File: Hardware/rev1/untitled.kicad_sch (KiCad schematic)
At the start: 16 parts, among them J2 USB_C_Receptacle_USB2.0_14P, J3 Screw_Terminal_01x02, U2 HT75xx-1-SOT89

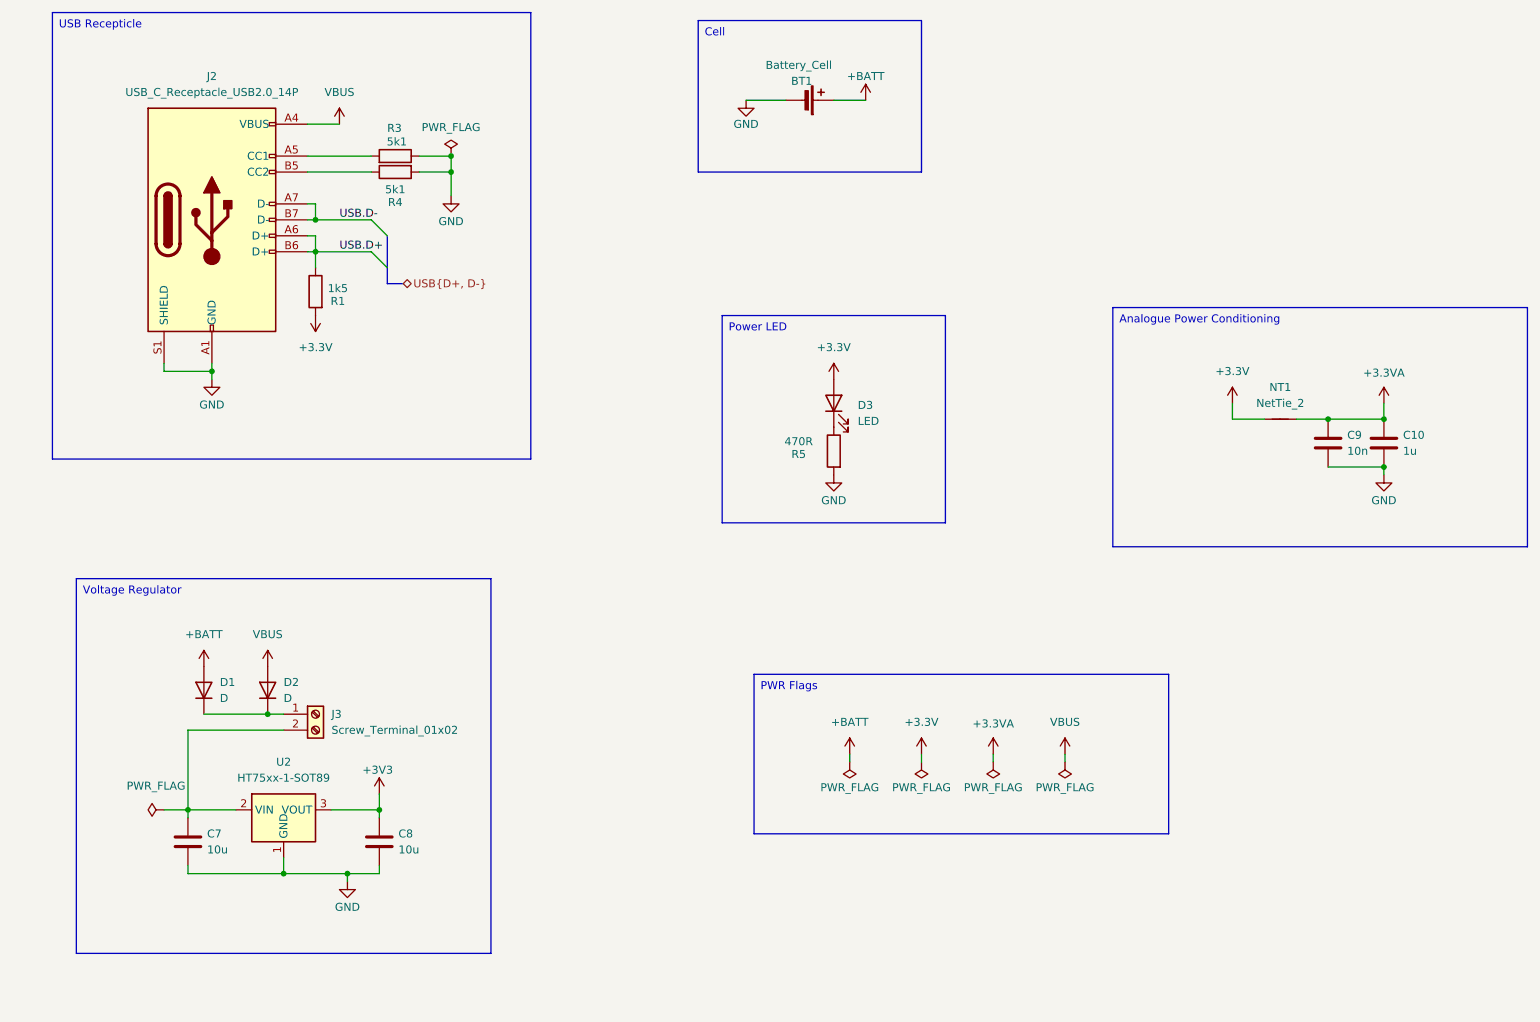
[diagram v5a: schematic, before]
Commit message: Literal Progress
PCB populated, schematic changed, all pins on MCU accessible from headers, all components on board, traces required
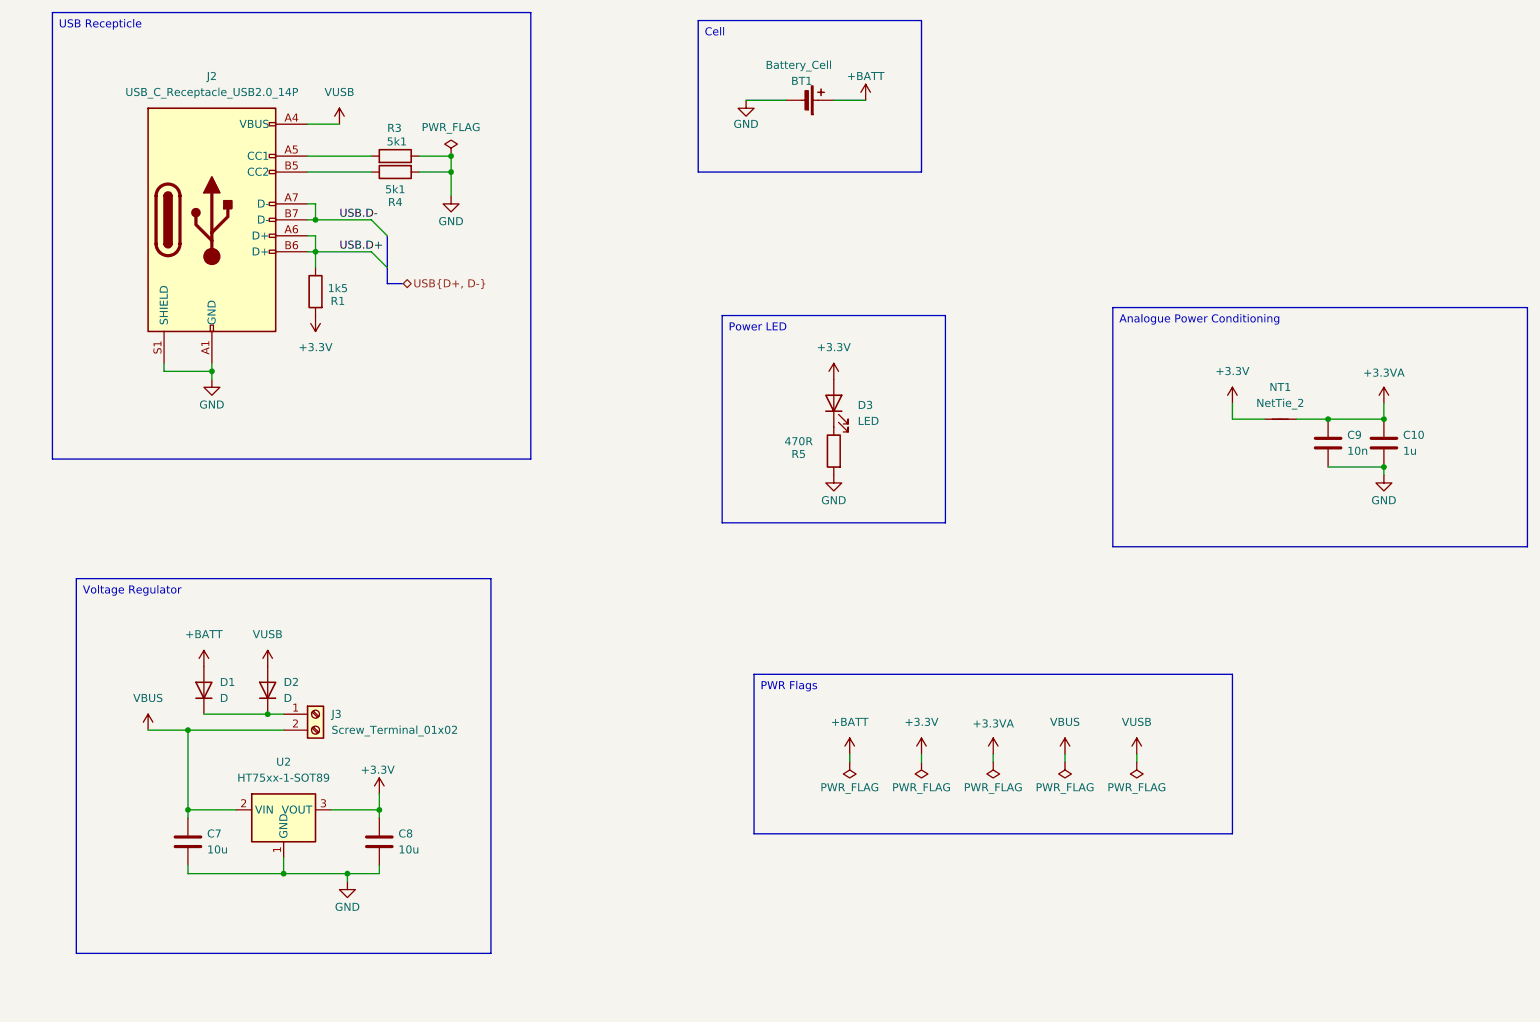
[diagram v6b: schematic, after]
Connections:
- net +3V3 is gone; now on net +3.3V: C8.1, U2.3 (VOUT)
- net VBUS: now also C7.1, J3.2 (Pin_2), U2.2 (VIN); no longer D2.2 (A), J2.A4 (VBUS), J2.A9 (VBUS), J2.B4 (VBUS), J2.B9 (VBUS)
- new net VUSB: D2.2 (A), J2.A4 (VBUS), J2.A9 (VBUS), J2.B4 (VBUS), J2.B9 (VBUS)
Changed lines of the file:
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@@
 	)
 	(junction
+		(at 54.61 140.97)
+		(diameter 0)
+		(color 0 0 0 0)
+	)
+	(junction
 		(at 85.09 153.67)
 		(diameter 0)
@@
 	(wire
 		(pts
+			(xy 205.74 144.78) (xy 205.74 146.05)
+		)
+		(stroke
+			(width 0)
+			(type default)
+		)
+	)
+	(wire
+		(pts
 			(xy 73.66 49.53) (xy 83.82 49.53)
 		)
@@
 	(wire
 		(pts
-			(xy 50.8 153.67) (xy 54.61 153.67)
-		)
-		(stroke
-			(width 0)
-			(type default)
-		)
-	)
-	(wire
-		(pts
 			(xy 50.8 83.82) (xy 58.42 83.82)
 		)
@@
 		)
 	)
+	(wire
+		(pts
+			(xy 48.26 140.97) (xy 54.61 140.97)
+		)
+		(stroke
+			(width 0)
+			(type default)
+		)
+	)
 	(text_box "Analogue Power Conditioning"
 		(exclude_from_sim no)
@@
 		(exclude_from_sim no)
 		(at 144.78 132.08 0)
-		(size 66.04 25.4)
+		(size 76.2 25.4)
 		(stroke
 			(width 0)
@@
 			)
 		)
-		(property "Value" "VBUS"
+		(property "Value" "VUSB"
 			(at 67.31 125.73 0)
 			(effects
@@
 			)
 		)
-		(property "Value" "+3V3"
+		(property "Value" "+3.3V"
 			(at 84.836 147.32 0)
 			(effects
@@
 	)
 	(symbol
-		(lib_id "power:PWR_FLAG")
-		(at 50.8 153.67 90)
-		(unit 1)
-		(exclude_from_sim no)
-		(in_bom yes)
-		(on_board yes)
-		(dnp no)
-		(fields_autoplaced yes)
-		(property "Reference" "#FLG01"
-			(at 48.895 153.67 0)
-			(effects
-				(font
-					(size 1.27 1.27)
-				)
-				(hide yes)
-			)
-		)
-		(property "Value" "PWR_FLAG"
-			(at 49.53 149.86 90)
-			(effects
-				(font
-					(size 1.27 1.27)
-				)
-			)
-		)
-		(property "Footprint" ""
-			(at 50.8 153.67 0)
-			(effects
-				(font
-					(size 1.27 1.27)
-				)
-				(hide yes)
-			)
-		)
-		(property "Datasheet" "~"
-			(at 50.8 153.67 0)
-			(effects
-				(font
-					(size 1.27 1.27)
-				)
-				(hide yes)
-			)
-		)
-		(property "Description" "Special symbol for telling ERC where power comes from"
-			(at 50.8 153.67 0)
-			(effects
-				(font
-					(size 1.27 1.27)
-				)
-				(hide yes)
-			)
-		)
-		(pin "1"
-		)
-		(instances
-			(project "rev1"
-				(path "/e52639ab-1647-4d34-8bc5-5aadc4708147/28e3f1a4-a9ec-420d-b6dc-1cdf5f0e43fa"
-					(reference "#FLG01")
-					(unit 1)
-				)
-			)
-		)
-	)
-	(symbol
 		(lib_id "power:+3.3V")
 		(at 157.48 85.09 0)
@@
 	)
 	(symbol
+		(lib_id "power:VBUS")
+		(at 48.26 140.97 0)
+		(unit 1)
+		(exclude_from_sim no)
+		(in_bom yes)
+		(on_board yes)
+		(dnp no)
+		(fields_autoplaced yes)
+		(property "Reference" "#PWR043"
+			(at 48.26 144.78 0)
+			(effects
+				(font
+					(size 1.27 1.27)
+				)
+				(hide yes)
+			)
+		)
+		(property "Value" "VBUS"
+			(at 48.26 135.89 0)
+			(effects
+				(font
+					(size 1.27 1.27)
+				)
+			)
+		)
+		(property "Footprint" ""
+			(at 48.26 140.97 0)
+			(effects
+				(font
+					(size 1.27 1.27)
+				)
+				(hide yes)
+			)
+		)
+		(property "Datasheet" ""
+			(at 48.26 140.97 0)
+			(effects
+				(font
+					(size 1.27 1.27)
+				)
+				(hide yes)
+			)
+		)
+		(property "Description" "Power symbol creates a global label with name \"VBUS\""
+			(at 48.26 140.97 0)
+			(effects
+				(font
+					(size 1.27 1.27)
+				)
+				(hide yes)
+			)
+		)
+		(pin "1"
+		)
+		(instances
+			(project "rev1"
+				(path "/e52639ab-1647-4d34-8bc5-5aadc4708147/28e3f1a4-a9ec-420d-b6dc-1cdf5f0e43fa"
+					(reference "#PWR043")
+					(unit 1)
+				)
+			)
+		)
+	)
+	(symbol
+		(lib_id "power:VBUS")
+		(at 205.74 144.78 0)
+		(unit 1)
+		(exclude_from_sim no)
+		(in_bom yes)
+		(on_board yes)
+		(dnp no)
+		(fields_autoplaced yes)
+		(property "Reference" "#PWR044"
+			(at 205.74 148.59 0)
+			(effects
+				(font
+					(size 1.27 1.27)
+				)
+				(hide yes)
+			)
+		)
+		(property "Value" "VUSB"
+			(at 205.74 139.7 0)
+			(effects
+				(font
+					(size 1.27 1.27)
+				)
+			)
+		)
+		(property "Footprint" ""
+			(at 205.74 144.78 0)
+			(effects
+				(font
+					(size 1.27 1.27)
+				)
+				(hide yes)
+			)
+		)
+		(property "Datasheet" ""
+			(at 205.74 144.78 0)
+			(effects
+				(font
+					(size 1.27 1.27)
+				)
+				(hide yes)
+			)
+		)
+		(property "Description" "Power symbol creates a global label with name \"VBUS\""
+			(at 205.74 144.78 0)
+			(effects
+				(font
+					(size 1.27 1.27)
+				)
+				(hide yes)
+			)
+		)
+		(pin "1"
+		)
+		(instances
+			(project "rev1"
+				(path "/e52639ab-1647-4d34-8bc5-5aadc4708147/28e3f1a4-a9ec-420d-b6dc-1cdf5f0e43fa"
+					(reference "#PWR044")
+					(unit 1)
+				)
+			)
+		)
+	)
+	(symbol
 		(lib_id "Device:R")
 		(at 157.48 96.52 0)
@@
 			)
 		)
-		(property "Value" "VBUS"
+		(property "Value" "VUSB"
 			(at 78.74 39.37 0)
 			(effects
@@
 					(unit 1)
 				)
+			)
+		)
+	)
+	(symbol
+		(lib_id "power:PWR_FLAG")
+		(at 205.74 146.05 180)
+		(unit 1)
+		(exclude_from_sim no)
+		(in_bom yes)
+		(on_board yes)
+		(dnp no)
+		(property "Reference" "#FLG07"
+			(at 205.74 147.955 0)
+			(effects
+				(font
+					(size 1.27 1.27)
+				)
+				(hide yes)
+			)
+		)
+		(property "Value" "PWR_FLAG"
+			(at 205.74 150.114 0)
+			(effects
+				(font
+					(size 1.27 1.27)
+				)
+			)
+		)
+		(property "Footprint" ""
+			(at 205.74 146.05 0)
+			(effects
+				(font
+					(size 1.27 1.27)
+				)
+				(hide yes)
+			)
+		)
+		(property "Datasheet" "~"
+			(at 205.74 146.05 0)
+			(effects
+				(font
+					(size 1.27 1.27)
+				)
+				(hide yes)
+			)
+		)
+		(property "Description" "Special symbol for telling ERC where power comes from"
+			(at 205.74 146.05 0)
+			(effects
+				(font
+					(size 1.27 1.27)
+				)
+				(hide yes)
+			)
+		)
+		(pin "1"
+		)
+		(instances
+			(project "rev1"
+				(path "/e52639ab-1647-4d34-8bc5-5aadc4708147/28e3f1a4-a9ec-420d-b6dc-1cdf5f0e43fa"
+					(reference "#FLG07")
+					(unit 1)
+				)

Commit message: No vallium for the whole week :(
Net tie footprint, moved breakouts, crystal we think is close enough, tried to look for debug interface but didn't find it. no vallies :(
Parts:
- NT1: footprint NetTie:NetTie-2_SMD_Pad2.0mm -> NetTie:NetTie-2_SMD_Pad0.5mm
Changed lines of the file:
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@@
 			)
 		)
-		(property "Footprint" "NetTie:NetTie-2_SMD_Pad2.0mm"
+		(property "Footprint" "NetTie:NetTie-2_SMD_Pad0.5mm"
 			(at 228.6 91.44 0)
 			(effects

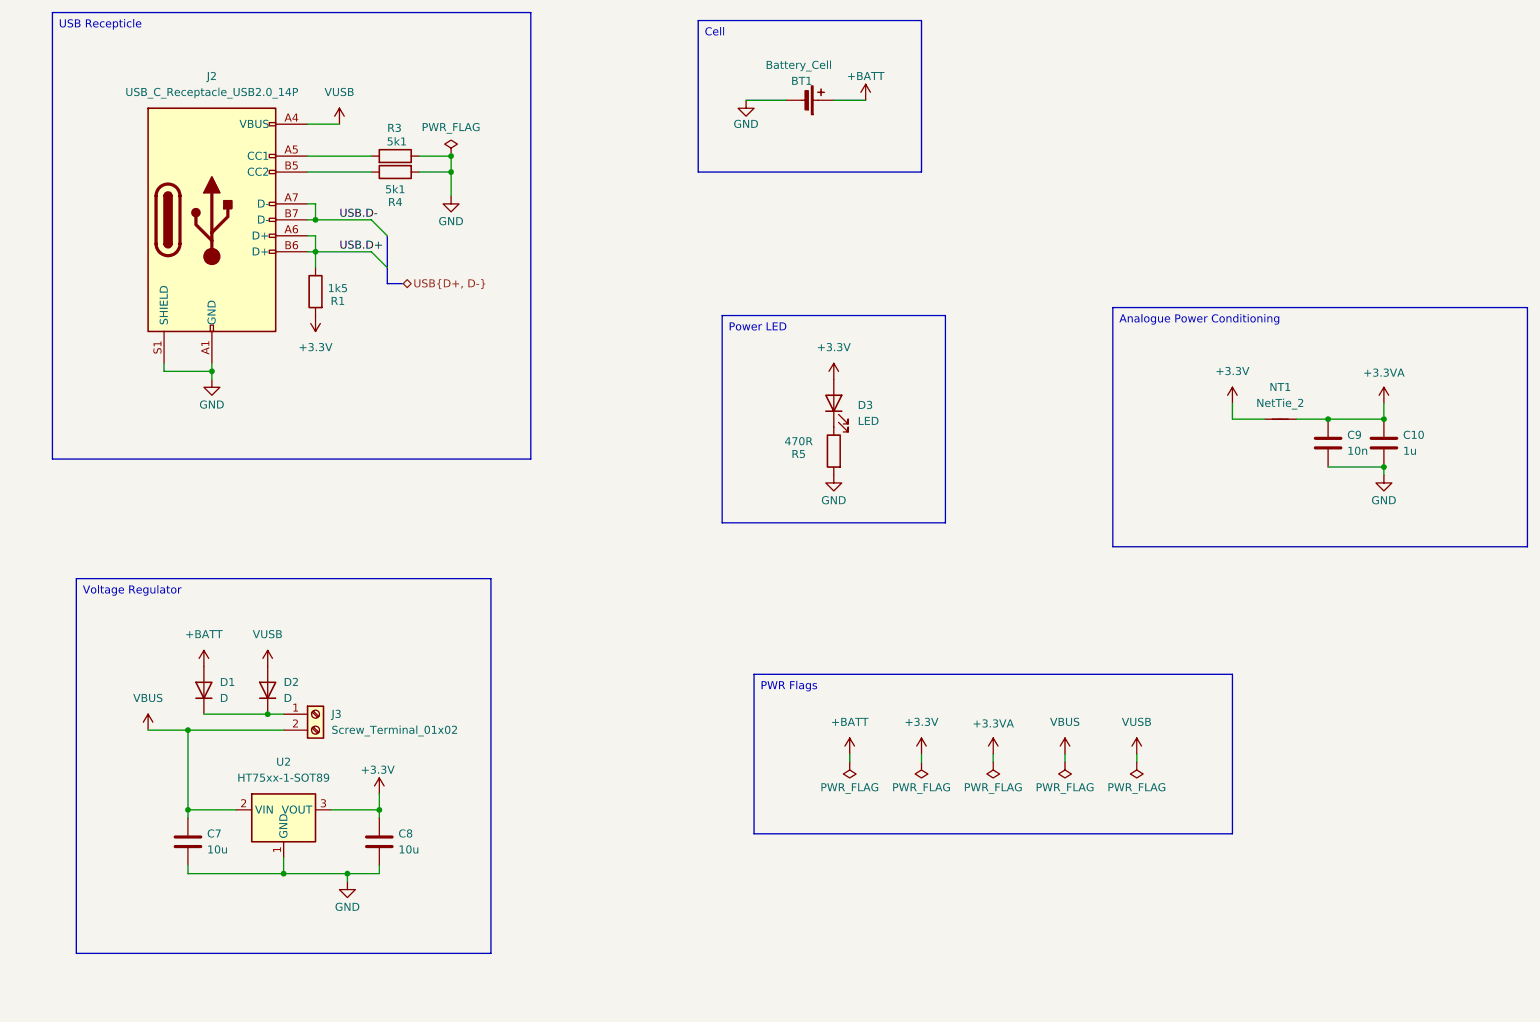
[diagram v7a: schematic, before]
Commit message: Updated traces, moved mounting hole, selected switching diodes for power regulation
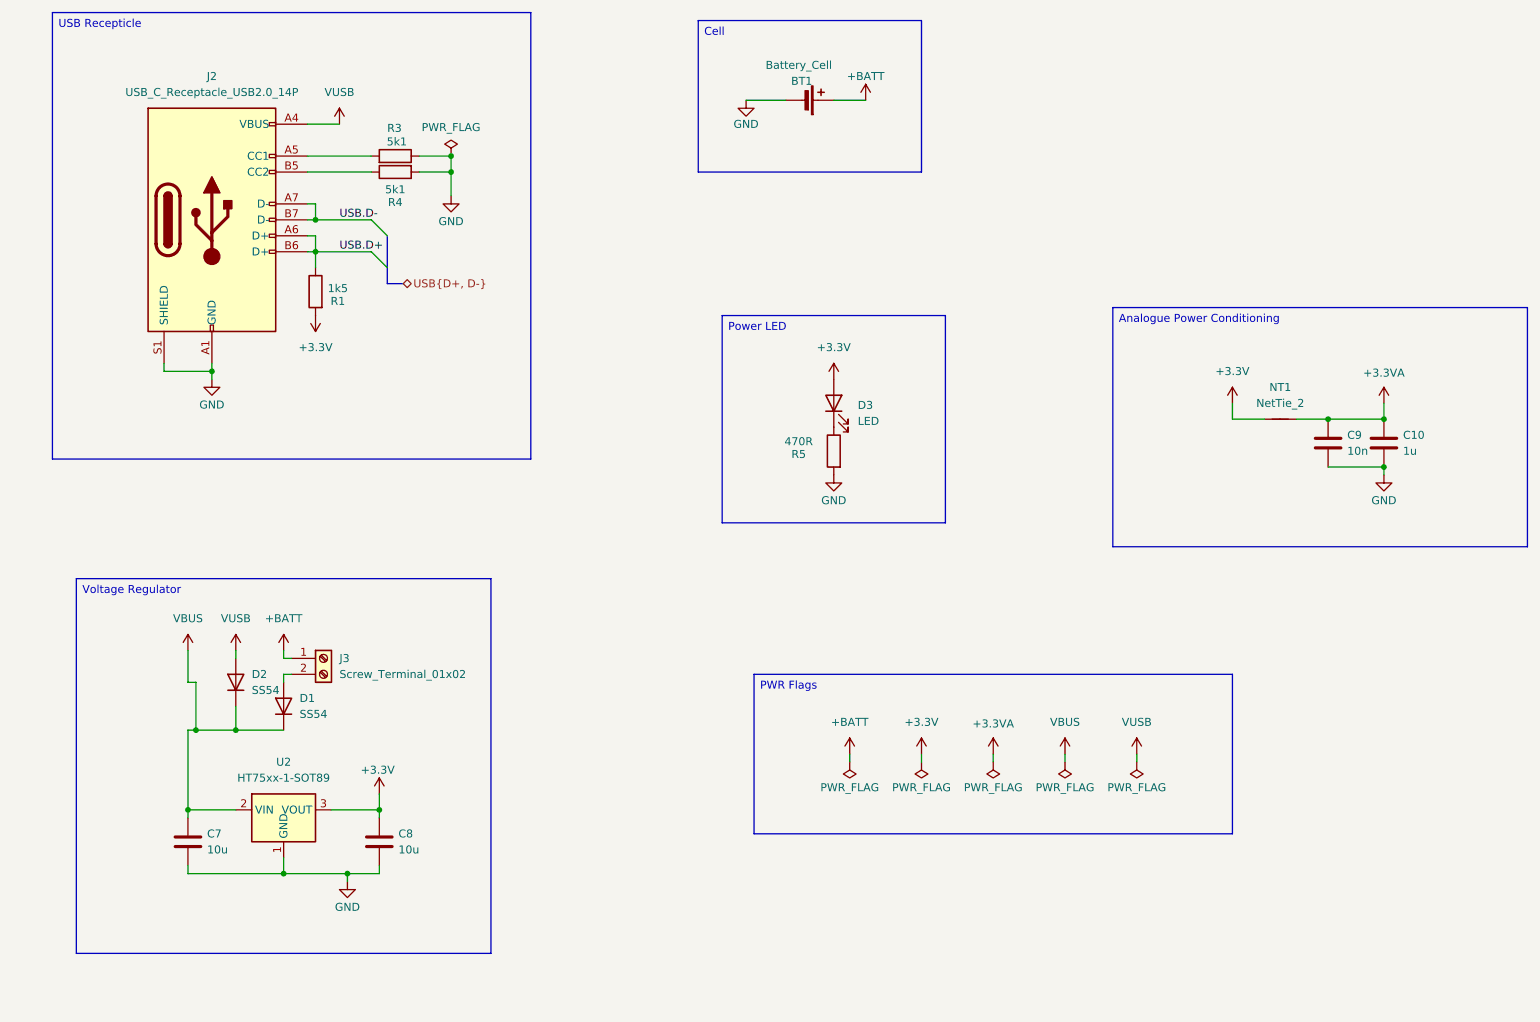
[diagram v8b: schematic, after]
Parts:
- D1, D2: value D -> SS54; footprint Diode_SMD:D_SOD-123F -> Diode_SMD:D_SMA; JLCPCB Part # (none) -> C22452
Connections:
- net +BATT: now also J3.1 (Pin_1); no longer D1.2 (A)
- net VBUS: now also D1.1 (K), D2.1 (K); no longer J3.2 (Pin_2)
- new net: D1.2 (A), J3.2 (Pin_2)
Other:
- moved on the sheet: D1, J3
